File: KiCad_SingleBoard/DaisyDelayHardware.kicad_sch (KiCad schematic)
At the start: 49 parts, among them J1 AUDIO_OUTPUT, J2 FEEDBACK_CV_INPUT, J3 DELAY_TIME_CV_INPUT, J5 AUDIO_INPUT, J6 Eurorack_Power_16pin_Shrouded, SW1 SW_SPDT, U1 LM4040DBZ-10, U2 TL074, U3 MCP6002-xP

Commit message: backup before pcb revision
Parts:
- C16: footprint Capacitor_THT:CP_Radial_D5.0mm_P2.50mm -> Capacitor_THT:CP_Radial_D8.0mm_P2.50mm
- RV1, RV2: footprint eurocad:Alpha9mmPot -> PCM_4ms_Potentiometer:Pot_9mm_DShaft
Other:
- note added: "Do we have 66.5K resistors?!?"
- note added: "Need op amp!"
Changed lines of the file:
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@@
 		)
 	)
+	(text "Do we have 66.5K resistors?!?"
+		(exclude_from_sim no)
+		(at 107.95 195.072 0)
+		(effects
+			(font
+				(size 1.27 1.27)
+			)
+		)
+	)
 	(text "Daisy Seed"
 		(exclude_from_sim no)
@@
 		)
 	)
+	(text "Need op amp!\n"
+		(exclude_from_sim no)
+		(at 100.33 192.024 0)
+		(effects
+			(font
+				(size 1.27 1.27)
+			)
+		)
+	)
 	(global_label "3V3_A"
 		(shape input)
@@
 			)
 		)
-		(property "Footprint" "Capacitor_THT:CP_Radial_D5.0mm_P2.50mm"
+		(property "Footprint" "Capacitor_THT:CP_Radial_D8.0mm_P2.50mm"
 			(at 139.3952 190.5 0)
 			(effects
@@
 			)
 		)
-		(property "Footprint" "eurocad:Alpha9mmPot"
+		(property "Footprint" "PCM_4ms_Potentiometer:Pot_9mm_DShaft"
 			(at 38.1 162.56 0)
 			(effects
@@
 			)
 		)
-		(property "Footprint" "eurocad:Alpha9mmPot"
+		(property "Footprint" "PCM_4ms_Potentiometer:Pot_9mm_DShaft"
 			(at 38.1 116.84 0)
 			(effects

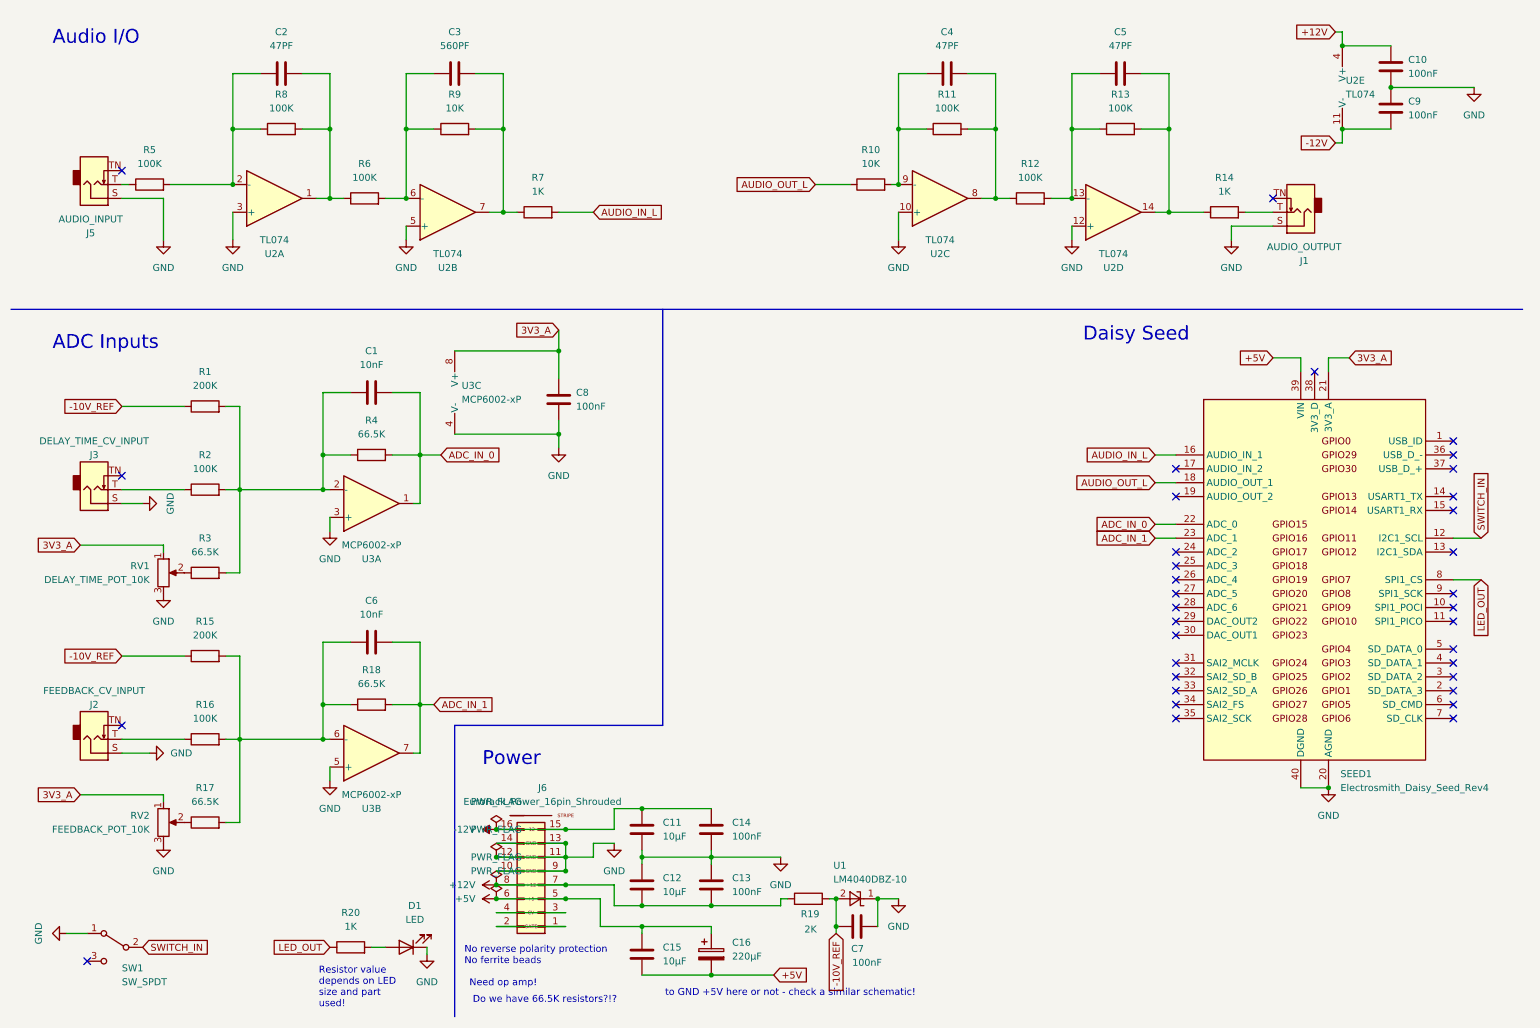
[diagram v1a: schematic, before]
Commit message: pcb revised - but doesn't meet jlcpcb design rules
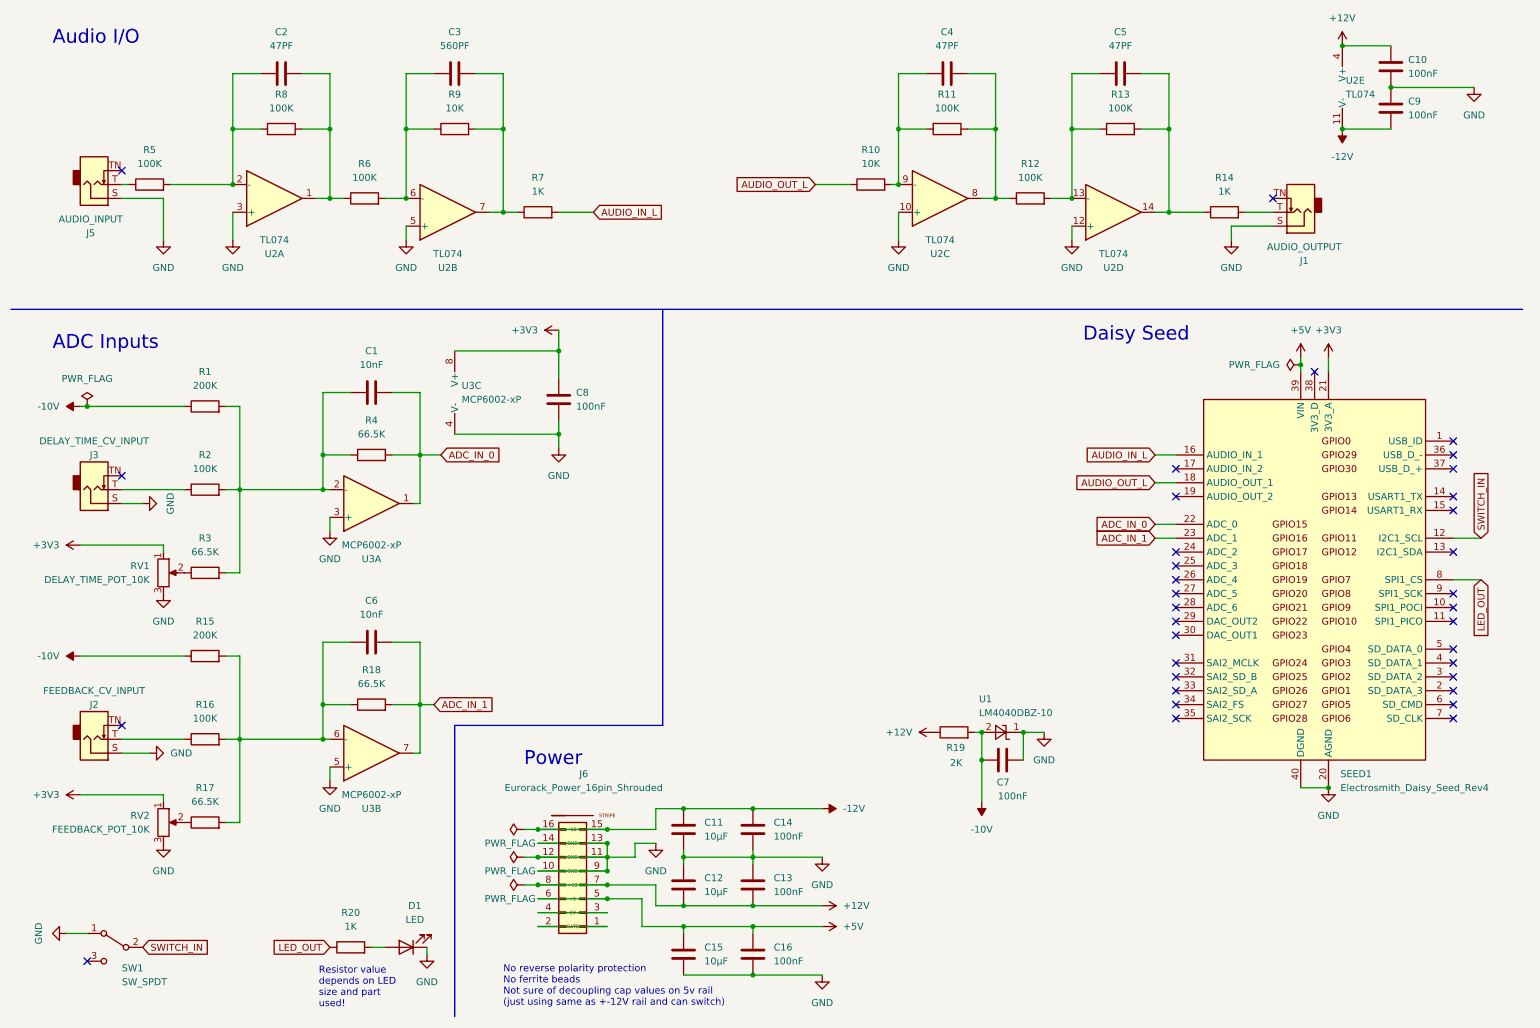
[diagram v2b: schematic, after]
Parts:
- removed C16: 220µF, Capacitor_THT:CP_Radial_D8.0mm_P2.50mm, symbol Device:C_Polarized
- added C16: 100nF, Capacitor_THT:C_Disc_D3.0mm_W1.6mm_P2.50mm, symbol Device:C
- R1, R10, R11, R12, R13, R14, R15, R16, R17, R18, R19, R2, R20, R3, R4, R5, R6, R7, R8, R9: footprint Resistor_THT:R_Axial_DIN0204_L3.6mm_D1.6mm_P5.08mm_Horizontal -> Resistor_THT:R_Axial_DIN0207_L6.3mm_D2.5mm_P7.62mm_Horizontal
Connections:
- net +5V: now also C16.1; no longer C15.2
- net GND: now also C15.2, C16.2
- net -10V_REF renamed -10V
- net 3V3_A renamed +3V3
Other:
- note added: "No reverse polarity protection No ferrite beads Not sure of decoupling cap values on 5v rail (just using same as +-12V rail and can switch)"
- note removed: "Do we have 66.5K resistors?!?"
- note removed: "Need op amp!"
- note removed: "No reverse polarity protection No ferrite beads"
- note removed: "to GND +5V here or not - check a similar schematic!"
- moved on the sheet: C11, C12, C13, C14, C15, J6

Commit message: latest updates
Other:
- note added: "To change to -12V"
- moved on the sheet: C8, U3C
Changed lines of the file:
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@@
 	)
 	(junction
-		(at 110.49 76.2)
+		(at 119.38 104.14)
 		(diameter 0)
 		(color 0 0 0 0)
@@
 	)
 	(junction
-		(at 110.49 91.44)
+		(at 119.38 119.38)
 		(diameter 0)
 		(color 0 0 0 0)
@@
 	(wire
 		(pts
-			(xy 110.49 76.2) (xy 110.49 72.39)
+			(xy 119.38 104.14) (xy 119.38 100.33)
 		)
 		(stroke
@@
 	(wire
 		(pts
-			(xy 110.49 88.9) (xy 110.49 91.44)
+			(xy 119.38 116.84) (xy 119.38 119.38)
 		)
 		(stroke
@@
 	(wire
 		(pts
-			(xy 91.44 91.44) (xy 110.49 91.44)
+			(xy 100.33 119.38) (xy 119.38 119.38)
 		)
 		(stroke
@@
 	(wire
 		(pts
-			(xy 110.49 76.2) (xy 110.49 81.28)
+			(xy 119.38 104.14) (xy 119.38 109.22)
 		)
 		(stroke
@@
 	(wire
 		(pts
-			(xy 91.44 76.2) (xy 110.49 76.2)
+			(xy 100.33 104.14) (xy 119.38 104.14)
 		)
 		(stroke
@@
 	(wire
 		(pts
-			(xy 110.49 91.44) (xy 110.49 93.98)
+			(xy 119.38 119.38) (xy 119.38 121.92)
 		)
 		(stroke
@@
 		)
 	)
+	(text "To change to -12V"
+		(exclude_from_sim no)
+		(at 171.958 141.986 0)
+		(effects
+			(font
+				(size 1.27 1.27)
+			)
+		)
+	)
 	(text "Daisy Seed"
 		(exclude_from_sim no)
@@
 	(symbol
 		(lib_id "power:+3V3")
-		(at 110.49 72.39 90)
+		(at 119.38 100.33 90)
 		(unit 1)
 		(exclude_from_sim no)
@@
 		(fields_autoplaced yes)
 		(property "Reference" "#PWR029"
-			(at 114.3 72.39 0)
+			(at 123.19 100.33 0)
 			(effects
 				(font
@@
 		)
 		(property "Value" "+3V3"
-			(at 106.68 72.3899 90)
+			(at 115.57 100.3299 90)
 			(effects
 				(font
@@
 		)
 		(property "Footprint" ""
-			(at 110.49 72.39 0)
+			(at 119.38 100.33 0)
 			(effects
 				(font
@@
 		)
 		(property "Datasheet" ""
-			(at 110.49 72.39 0)
+			(at 119.38 100.33 0)
 			(effects
 				(font
@@
 		)
 		(property "Description" "Power symbol creates a global label with name \"+3V3\""
-			(at 110.49 72.39 0)
+			(at 119.38 100.33 0)
 			(effects
 				(font
@@
 		(lib_name "GND_3")
 		(lib_id "power:GND")
-		(at 110.49 93.98 0)
+		(at 119.38 121.92 0)
 		(unit 1)
 		(exclude_from_sim no)
@@
 		(dnp no)
 		(property "Reference" "#PWR08"
-			(at 110.49 100.33 0)
+			(at 119.38 128.27 0)
 			(effects
 				(font
@@
 		)
 		(property "Value" "GND"
-			(at 110.49 99.06 0)
+			(at 119.38 127 0)
 			(effects
 				(font
@@
 		)
 		(property "Footprint" ""
-			(at 110.49 93.98 0)
+			(at 119.38 121.92 0)
 			(effects
 				(font
@@
 		)
 		(property "Datasheet" ""
-			(at 110.49 93.98 0)
+			(at 119.38 121.92 0)
 			(effects
 				(font
@@
 		)
 		(property "Description" "Power symbol creates a global label with name \"GND\" , ground"
-			(at 110.49 93.98 0)
+			(at 119.38 121.92 0)
 			(effects
 				(font
@@
 	(symbol
 		(lib_id "Device:C")
-		(at 110.49 85.09 0)
+		(at 119.38 113.03 0)
 		(unit 1)
 		(exclude_from_sim no)
@@
 		(fields_autoplaced yes)
 		(property "Reference" "C8"
-			(at 113.665 83.82 0)
+			(at 122.555 111.76 0)
 			(effects
 				(font
@@
 		)
 		(property "Value" "100nF"
-			(at 113.665 86.36 0)
+			(at 122.555 114.3 0)
 			(effects
 				(font
@@
 		)
 		(property "Footprint" "Capacitor_THT:C_Disc_D3.0mm_W1.6mm_P2.50mm"
-			(at 111.4552 88.9 0)
+			(at 120.3452 116.84 0)
 			(effects
 				(font
@@
 		)
 		(property "Datasheet" "~"
-			(at 110.49 85.09 0)
+			(at 119.38 113.03 0)
 			(effects
 				(font
@@
 		)
 		(property "Description" ""
-			(at 110.49 85.09 0)
+			(at 119.38 113.03 0)
 			(effects
 				(font
@@
 	(symbol
 		(lib_id "Amplifier_Operational:MCP6002-xP")
-		(at 93.98 83.82 0)
+		(at 102.87 111.76 0)
 		(unit 3)
 		(exclude_from_sim no)
@@
 		(on_board yes)
 		(dnp no)
-		(fields_autoplaced yes)
 		(property "Reference" "U3"
-			(at 92.71 82.5499 0)
+			(at 101.6 110.4899 0)
 			(effects
 				(font
@@
 		)
 		(property "Value" "MCP6002-xP"
-			(at 92.71 85.0899 0)
+			(at 101.6 113.0299 0)
 			(effects
 				(font
@@
 		)
 		(property "Footprint" "Package_DIP:DIP-8_W7.62mm"
-			(at 93.98 83.82 0)
+			(at 102.87 111.76 0)
 			(effects
 				(font
@@
 		)
 		(property "Datasheet" "http://ww1.microchip.com/downloads/en/DeviceDoc/21733j.pdf"
-			(at 93.98 83.82 0)
+			(at 102.87 111.76 0)
 			(effects
 				(font
@@
 		)
 		(property "Description" "1MHz, Low-Power Op Amp, DIP-8"
-			(at 93.98 83.82 0)
+			(at 102.87 111.76 0)
 			(effects
 				(font
